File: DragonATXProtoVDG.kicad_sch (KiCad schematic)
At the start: 59 parts, among them IC1 74LS273, J3 JTAG, U1 AD724JR, U2 74LS244, U3 ATF1508AS-10JI84, U4 74LS244, U5 74LS244, Y2 4.433618MHz

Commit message: resolve routing
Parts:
- added C1: 10uF, Capacitor_SMD:CP_Elec_4x5.4, symbol Device:C_Polarized_Small
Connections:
- net CLK is gone; now on net VCLK: U3.33 (I/O)
- net +5V: now also C1.1
- net BLUE: now also TP1.1
- net GND: now also C1.2
- net GREEN: now also TP3.1
- net RED: now also TP2.1
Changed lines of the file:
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@@
 	)
 	(junction
+		(at 198.12 48.26)
+		(diameter 0)
+		(color 0 0 0 0)
+	)
+	(junction
 		(at 205.74 26.67)
 		(diameter 0)
@@
 	(wire
 		(pts
+			(xy 198.12 38.1) (xy 198.12 48.26)
+		)
+		(stroke
+			(width 0)
+			(type default)
+		)
+	)
+	(wire
+		(pts
 			(xy 339.09 203.2) (xy 340.36 203.2)
 		)
@@
 	(wire
 		(pts
+			(xy 205.74 38.1) (xy 208.28 38.1)
+		)
+		(stroke
+			(width 0)
+			(type default)
+		)
+	)
+	(wire
+		(pts
 			(xy 100.33 35.56) (xy 105.41 35.56)
 		)
@@
 	(wire
 		(pts
+			(xy 200.66 38.1) (xy 198.12 38.1)
+		)
+		(stroke
+			(width 0)
+			(type default)
+		)
+	)
+	(wire
+		(pts
 			(xy 96.52 43.18) (xy 105.41 43.18)
 		)
@@
 	(wire
 		(pts
-			(xy 208.28 48.006) (xy 208.28 48.26)
+			(xy 208.28 38.1) (xy 208.28 48.26)
 		)
 		(stroke
@@
 	(wire
 		(pts
-			(xy 200.66 48.26) (xy 196.85 48.26)
+			(xy 200.66 48.26) (xy 198.12 48.26)
 		)
 		(stroke
@@
 		)
 	)
+	(label "VCLK"
+		(at 163.83 162.56 180)
+		(effects
+			(font
+				(size 1.27 1.27)
+			)
+			(justify right bottom)
+		)
+	)
 	(label "~{A}{slash}S"
 		(at 185.42 57.15 180)
@@
 		)
 	)
+	(global_label "BLUE"
+		(shape input)
+		(at 265.43 259.08 180)
+		(fields_autoplaced yes)
+		(effects
+			(font
+				(size 1.27 1.27)
+			)
+			(justify right)
+		)
+		(property "Intersheetrefs" "${INTERSHEET_REFS}"
+			(at 257.6672 259.08 0)
+			(effects
+				(font
+					(size 1.27 1.27)
+				)
+				(justify right)
+				(hide yes)
+			)
+		)
+	)
 	(global_label "TDI"
 		(shape input)
@@
 		)
 	)
+	(global_label "RED"
+		(shape input)
+		(at 265.43 264.16 180)
+		(fields_autoplaced yes)
+		(effects
+			(font
+				(size 1.27 1.27)
+			)
+			(justify right)
+		)
+		(property "Intersheetrefs" "${INTERSHEET_REFS}"
+			(at 258.7558 264.16 0)
+			(effects
+				(font
+					(size 1.27 1.27)
+				)
+				(justify right)
+				(hide yes)
+			)
+		)
+	)
 	(global_label "~{RESET}"
 		(shape output)
@@
 		)
 	)
+	(global_label "GREEN"
+		(shape input)
+		(at 265.43 269.24 180)
+		(fields_autoplaced yes)
+		(effects
+			(font
+				(size 1.27 1.27)
+			)
+			(justify right)
+		)
+		(property "Intersheetrefs" "${INTERSHEET_REFS}"
+			(at 256.2763 269.24 0)
+			(effects
+				(font
+					(size 1.27 1.27)
+				)
+				(justify right)
+				(hide yes)
+			)
+		)
+	)
 	(global_label "Chroma"
 		(shape bidirectional)
@@
 		)
 	)
-	(global_label "CLK"
-		(shape input)
-		(at 163.83 162.56 180)
-		(fields_autoplaced yes)
-		(effects
-			(font
-				(size 1.27 1.27)
-			)
-			(justify right)
-		)
-		(property "Intersheetrefs" "${INTERSHEET_REFS}"
-			(at 157.9377 162.4806 0)
-			(effects
-				(font
-					(size 1.27 1.27)
-				)
-				(justify right)
-				(hide yes)
-			)
-		)
-	)
 	(global_label "TDO"
 		(shape output)
@@
 	(symbol
 		(lib_id "power:+5V")
-		(at 196.85 48.26 180)
+		(at 198.12 48.26 180)
 		(unit 1)
 		(exclude_from_sim no)
@@
 		(fields_autoplaced yes)
 		(property "Reference" "#PWR010"
-			(at 196.85 44.45 0)
+			(at 198.12 44.45 0)
 			(effects
 				(font
@@
 		)
 		(property "Value" "+5V"
-			(at 196.85 53.594 0)
+			(at 198.12 53.594 0)
 			(effects
 				(font
@@
 		)
 		(property "Footprint" ""
-			(at 196.85 48.26 0)
+			(at 198.12 48.26 0)
 			(effects
 				(font
@@
 		)
 		(property "Datasheet" ""
-			(at 196.85 48.26 0)
+			(at 198.12 48.26 0)
 			(effects
 				(font
@@
 		)
 		(property "Description" ""
-			(at 196.85 48.26 0)
+			(at 198.12 48.26 0)
 			(effects
 				(font
@@
 					(unit 1)
 				)
+			)
+		)
+	)
+	(symbol
+		(lib_id "Device:C_Polarized_Small")
+		(at 203.2 38.1 90)
+		(mirror x)
+		(unit 1)
+		(exclude_from_sim no)
+		(in_bom yes)
+		(on_board yes)
+		(dnp no)
+		(fields_autoplaced yes)
+		(property "Reference" "C1"
+			(at 202.6539 45.085 90)
+			(effects
+				(font
+					(size 1.27 1.27)
+				)
+			)
+		)
+		(property "Value" "10uF"
+			(at 202.6539 42.545 90)
+			(effects
+				(font
+					(size 1.27 1.27)
+				)
+			)
+		)
+		(property "Footprint" "Capacitor_SMD:CP_Elec_4x5.4"
+			(at 203.2 38.1 0)
+			(effects
+				(font
+					(size 1.27 1.27)
+				)
+				(hide yes)
+			)
+		)
+		(property "Datasheet" "https://www.we-online.com/katalog/datasheet/860010372006.pdf"
+			(at 203.2 38.1 0)
+			(effects
+				(font
+					(size 1.27 1.27)
+				)
+				(hide yes)
+			)
+		)
+		(property "Description" ""
+			(at 203.2 38.1 0)
+			(effects
+				(font
+					(size 1.27 1.27)
+				)
+				(hide yes)
+			)
+		)
+		(property "DigiKey" "732-8254-1-ND"
+			(at 203.2 38.1 0)
+			(effects
+				(font
+					(size 1.27 1.27)
+				)
+				(hide yes)
+			)
+		)
+		(pin "1"
+		)
+		(pin "2"
+		)
+		(instances
+			(project "DragonATXProtoVDG"
+				(path "/ecdc7bf3-2e40-49cd-bc4c-ef5d00bcfe42"
+					(reference "C1")
+					(unit 1)
+				)

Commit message: rework layout
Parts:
- removed C14, C20, C9: 0.1uF, Capacitor_SMD:C_0805_2012Metric_Pad1.18x1.45mm_HandSolder, symbol Device:C_Small
- removed unit 2 of PL1
- removed U2, U4, U5: 74LS244, PCM_Package_SO_AKL:SO-20_5.3x12.6mm_P1.27mm, symbol 74xx:74LS244
- added R24: 4K7, PCM_Resistor_SMD_AKL:R_0805_2012Metric_Pad1.15x1.40mm_HandSolder, symbol Device:R_Small
- added TP5: VCC, TestPoint:TestPoint_Loop_D2.54mm_Drill1.5mm_Beaded, symbol Connector:TestPoint
- added TP6: VSS, TestPoint:TestPoint_Loop_D2.54mm_Drill1.5mm_Beaded, symbol Connector:TestPoint
- added Y3: 100MHz, Oscillator:Oscillator_SMD_SeikoEpson_SG8002LB-4Pin_5.0x3.2mm_HandSoldering, symbol Oscillator:ASV-xxxMHz
- PL1: footprint Library:Card_Edge -> Library:Card_Edge_Short; symbol Library:Card_Edge -> Library:Card_Edge_Short
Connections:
- net +5V: now also Y2.4 (Vdd), TP5.1, Y3.4 (Vdd)
- net A0: no longer U3.30 (I/O)
- net A1: no longer U3.31 (I/O)
- net CAS: no longer U3.24 (I/O)
- net E: no longer U3.80 (I/O)
- net GND: now also R24.2, TP6.1, Y3.2 (GND); no longer Y2.4 (Vdd)
- net INV: now also IC1.15 (Q5)
- net Q: no longer U3.79 (I/O)
- net Q0: now also IC1.2 (Q0)
- net Q1: now also IC1.5 (Q1)
- net Q2: now also IC1.6 (Q2)
- net Q3: now also IC1.9 (Q3)
- net Q4: now also IC1.19 (Q7)
- net Q5: now also IC1.16 (Q6)
- net Q7: now also IC1.12 (Q4)
- net RAS: no longer U3.25 (I/O)
- net R/W: no longer U3.77 (I/O)
- net ~{I}/E: now reaches U3.37 (I/O)
- net ~{I}/E: now also R24.1
- net ~{RP}: now reaches U3.6 (I/O)
- net at U3.83 (INPUT/GCLK1): now also Y3.3 (OUT)
- no-connect marks 45 -> 50

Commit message: refine board design
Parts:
- added J1: Conn_Coaxial, Library:Connector_RCA, symbol Connector:Conn_Coaxial
- added TP10: TestPoint_RowResetPulse, TestPoint:TestPoint_Pad_D1.0mm, symbol Connector:TestPoint_Probe
- added TP11: TestPoint_DA0, TestPoint:TestPoint_Pad_D1.0mm, symbol Connector:TestPoint_Probe
- added TP7: TestPoint_ColourClock, TestPoint:TestPoint_Pad_D1.0mm, symbol Connector:TestPoint_Probe
- added TP8: TestPoint_PixelClock, TestPoint:TestPoint_Pad_D1.0mm, symbol Connector:TestPoint_Probe
- added TP9: TestPoint_ReqFormat, TestPoint:TestPoint_Pad_D1.0mm, symbol Connector:TestPoint_Probe
- C15, C5, C6: footprint Capacitor_Tantalum_SMD:CP_EIA-3216-12_Kemet-S -> Capacitor_Tantalum_SMD:CP_EIA-6032-15_Kemet-U; DigiKey 478-4922-1-ND -> 478-1768-1-ND
- Y3: footprint Oscillator:Oscillator_SMD_SeikoEpson_SG8002LB-4Pin_5.0x3.2mm_HandSoldering -> Crystal:Crystal_SMD_7050-4Pin_7.0x5.0mm
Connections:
- net Composite: now also J1.1 (In)
- net DA0: now also TP11.1
- net FMT_CLOCK: now also TP7.1
- net Format: now also TP9.1
- net GND: now also J1.2 (Ext)
- net VCLK: now also TP8.1
- net ~{RP}: now also TP10.1
- net DA1: now reaches U3.22 (I/O)
- net DA2: now reaches U3.24 (I/O)
- net DA3: now reaches U3.25 (I/O)
- net DA4: now reaches U3.30 (I/O)
- net DA5: now reaches U3.31 (I/O)
- net DA6: now reaches U3.35 (I/O)
- net DA7: now reaches U3.36 (I/O)
- net DA8: now reaches U3.39 (I/O)
- net DA9: now reaches U3.40 (I/O)
- net DA10: now reaches U3.41 (I/O)
- net DA11: now reaches U3.48 (I/O)
- net DA12: now reaches U3.49 (I/O)
- no-connect marks 50 -> 38
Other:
- moved on the sheet: TP1, TP2, TP3, TP4

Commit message: revise for 1.0.7
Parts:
- added C11, C12, C9: 0.1uF, Capacitor_SMD:C_0805_2012Metric_Pad1.18x1.45mm_HandSolder, symbol Device:C_Small
- added R25, R26, R27: 75R, PCM_Resistor_SMD_AKL:R_0805_2012Metric_Pad1.15x1.40mm_HandSolder, symbol Device:R_Small
- added R28, R29, R30, R31, R32: 68R, PCM_Resistor_SMD_AKL:R_0805_2012Metric_Pad1.15x1.40mm_HandSolder, symbol Device:R_Small
- added R33, R34, R35: 150R, PCM_Resistor_SMD_AKL:R_0805_2012Metric_Pad1.15x1.40mm_HandSolder, symbol Device:R_Small
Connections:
- net BLUE: now also R32.1, R33.2; no longer R18.2, R22.1, U1.8 (BLUE)
- net GND: now also R25.1, R26.1, R27.1
- net GREEN: now also R31.1, R34.2; no longer R12.2, R16.1, U1.7 (GREEN)
- net RED: now also R30.1, R35.2; no longer R5.1, R8.2, U1.6 (RED)
- net ~{FS}: now also R28.2; no longer U1.15 (VSYNC)
- net ~{HS}: now also R29.2; no longer U1.16 (HSYNC)
- new net: R30.2, R5.1, R8.2
- new net: R18.2, R22.1, R32.2
- new net: R12.2, R16.1, R31.2
- new net: C9.1, R25.2, R35.1
- new net: C11.1, R26.2, R34.1
- new net: R28.1, U1.15 (VSYNC)
- new net: C11.2, U1.7 (GREEN)
- new net: R29.1, U1.16 (HSYNC)
- new net: C9.2, U1.6 (RED)
- new net: C12.2, U1.8 (BLUE)
- new net: C12.1, R27.2, R33.1
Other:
- moved on the sheet: R10, R11, R12, R13, R14, R15, R16, R17, R18, R19, R20, R21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

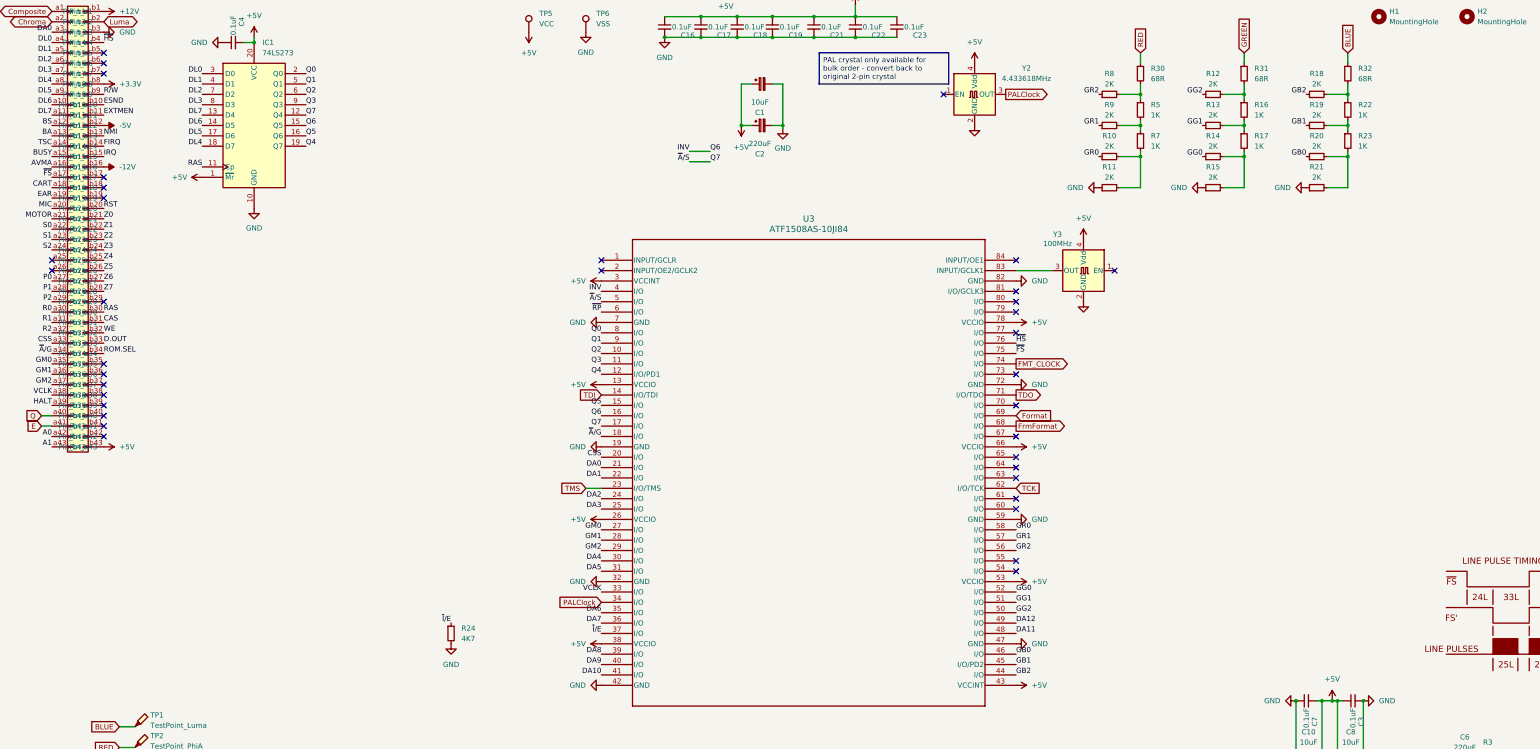
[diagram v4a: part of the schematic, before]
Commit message: redesign for character rom
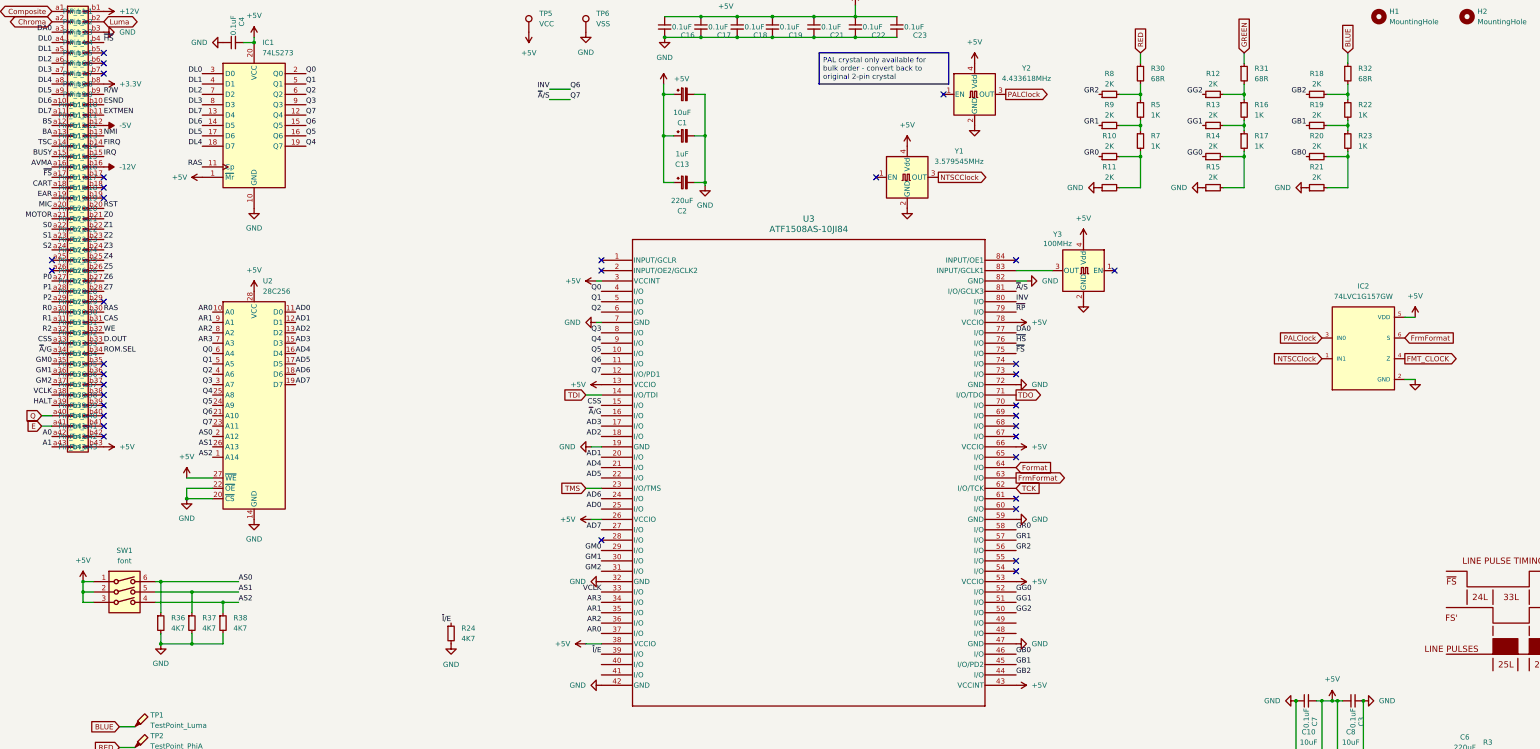
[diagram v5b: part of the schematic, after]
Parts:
- added C13: 1uF, Capacitor_SMD:CP_Elec_4x4.5, symbol Device:C_Polarized_Small
- added IC2: 74LVC1G157GW, Package_TO_SOT_SMD:SOT-363_SC-70-6_Handsoldering, symbol Library:NC7SZ157P6X
- added R36, R37, R38: 4K7, PCM_Resistor_SMD_AKL:R_0805_2012Metric_Pad1.15x1.40mm_HandSolder, symbol Device:R_Small
- added SW1: font, Button_Switch_THT:SW_DIP_SPSTx03_Slide_9.78x9.8mm_W7.62mm_P2.54mm, symbol Switch:SW_DIP_x03
- added U2: 28C256, Package_DIP:DIP-28_W15.24mm, symbol Memory_EEPROM:28C256
- added Y1: 3.579545MHz, Crystal:Crystal_SMD_7050-4Pin_7.0x5.0mm, symbol Oscillator:ASV-xxxMHz
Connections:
- net DA4 is gone; now on net GM1: U3.30 (I/O)
- net DA5 is gone; now on net GM2: U3.31 (I/O)
- net DA8 is gone; now on net ~{I}/E: U3.39 (I/O)
- net +5V: now also C13.1, IC2.5 (VDD), SW1.1, SW1.2, SW1.3, U2.27 (~{WE}), U2.28 (VCC), Y1.4 (Vdd)
- net CSS: now also U3.15 (I/O); no longer U3.20 (I/O)
- net DA0: now also U3.77 (I/O); no longer U3.21 (I/O)
- net FMT_CLOCK: now also IC2.4 (Z); no longer U3.74 (I/O)
- net Format: now also U3.64 (I/O); no longer U3.69 (I/O)
- net FrmFormat: now also U3.63 (I/O), IC2.6 (S); no longer U3.68 (I/O)
- net GM0: now also U3.29 (I/O); no longer U3.27 (I/O)
- net GM1: no longer U3.28 (I/O)
- net GM2: no longer U3.29 (I/O)
- net GND: now also C13.2, IC2.2 (GND), R36.2, R37.2, R38.2, U2.14 (GND), U2.20 (~{CS}), U2.22 (~{OE}), Y1.2 (GND)
- net INV: now also U3.11 (I/O), U3.80 (I/O), U2.21 (A10); no longer U3.16 (I/O), U3.4 (I/O)
- net PALClock: now also IC2.3 (IN0); no longer U3.34 (I/O)
- net Q0: now also U3.4 (I/O), U2.6 (A4); no longer U3.8 (I/O)
- net Q1: now also U3.5 (I/O), U2.5 (A5); no longer U3.9 (I/O)
- net Q2: now also U3.6 (I/O), U2.4 (A6); no longer U3.10 (I/O)
- net Q3: now also U3.8 (I/O), U2.3 (A7); no longer U3.11 (I/O)
- net Q4: now also U3.9 (I/O), U2.25 (A8); no longer U3.12 (I/O/PD1)
- net Q5: now also U3.10 (I/O), U2.24 (A9); no longer U3.15 (I/O)
- net Q7: now also U3.12 (I/O/PD1), U3.81 (I/O/GCLK3), U2.23 (A11); no longer U3.17 (I/O), U3.5 (I/O)
- net ~{A}/G: now also U3.16 (I/O); no longer U3.18 (I/O)
- net ~{I}/E: no longer U3.37 (I/O)
- net ~{RP}: now also U3.79 (I/O); no longer U3.6 (I/O)
- net DA1 renamed AD5
- net AD5: now also U2.17 (D5)
- net DA10: no longer names the net of U3.41 (I/O)
- net DA11: no longer names the net of U3.48 (I/O)
- net DA12: no longer names the net of U3.49 (I/O)
- net DA2 renamed AD6
- net AD6: now also U2.18 (D6)
- net DA3 renamed AD0
- net AD0: now also U2.11 (D0)
- net DA6 renamed AR1
- net AR1: now also U2.9 (A1)
- net DA7 renamed AR2
- net AR2: now also U2.8 (A2)
- net DA9: no longer names the net of U3.40 (I/O)
- new net AD1: U2.12 (D1), U3.20 (I/O)
- new net AD2: U2.13 (D2), U3.18 (I/O)
- new net AD3: U2.15 (D3), U3.17 (I/O)
- new net AD4: U2.16 (D4), U3.21 (I/O)
- new net AD7: U2.19 (D7), U3.27 (I/O)
- new net AR0: U2.10 (A0), U3.37 (I/O)
- new net AR3: U2.7 (A3), U3.34 (I/O)
- new net AS0: R36.1, SW1.6, U2.2 (A12)
- new net AS1: R37.1, SW1.5, U2.26 (A13)
- new net AS2: R38.1, SW1.4, U2.1 (A14)
- new net NTSCClock: IC2.1 (IN1), Y1.3 (OUT)
- no-connect marks 38 -> 37
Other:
- moved on the sheet: C1, C2
